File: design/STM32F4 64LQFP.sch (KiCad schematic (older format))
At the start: 15 parts, among them P2 SWD, U1 STM32F40X_LQFP64, X2 8MHz 10ppm

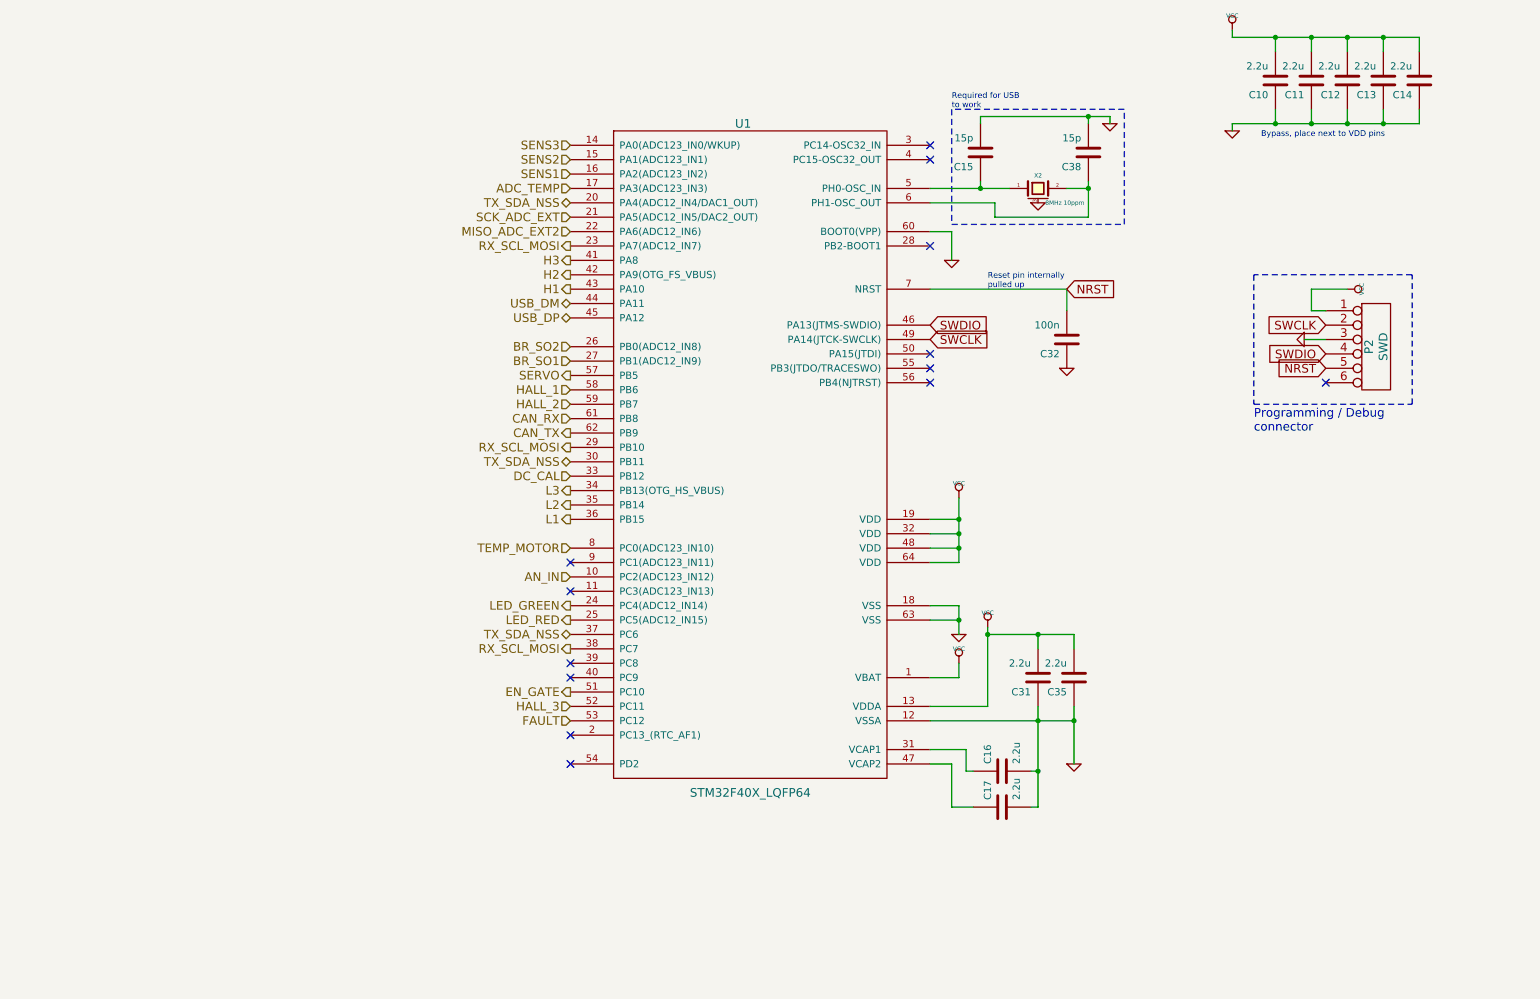
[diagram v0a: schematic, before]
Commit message: schema mods done
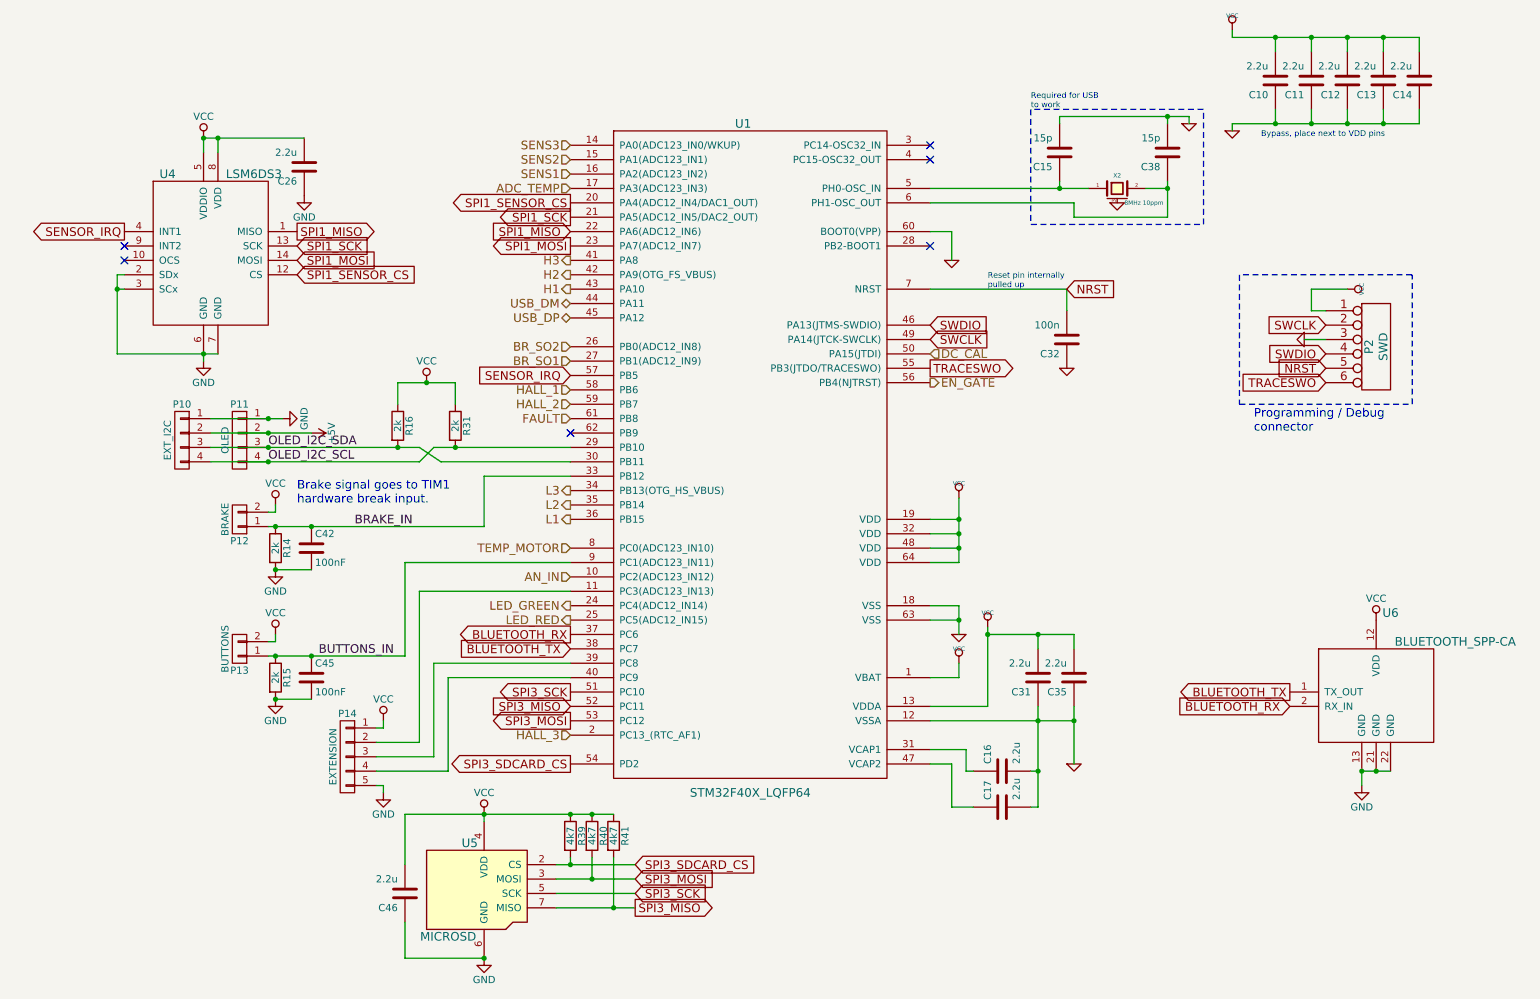
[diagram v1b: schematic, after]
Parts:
- added C26, C46: 2.2u, CRF1:SMD-0603_c, symbol C-RESCUE-BLDC_4
- added C42, C45: 100nF, symbol C
- added P10: EXT_I2C, symbol CONN_01X04
- added P11: OLED, symbol CONN_01X04
- added P12: BRAKE, symbol CONN_01X02
- added P13: BUTTONS, symbol CONN_01X02
- added P14: EXTENSION, symbol CONN_01X05
- added R14, R15, R16, R31: 2k, symbol R
- added R39, R40, R41: 4k7, symbol R
- added U4: LSM6DS3, symbol LSM6DS3
- added U5: MICROSD, symbol MICROSD
- added U6: BLUETOOTH_SPP-CA, symbol BLUETOOTH_SPP-CA
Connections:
- net CAN_RX is gone; now on net FAULT: U1.61 (PB8)
- net DC_CAL: now also U1.50 (PA15(JTDI)); no longer U1.33 (PB12)
- net EN_GATE: now also U1.56 (PB4(NJTRST)); no longer U1.51 (PC10)
- net FAULT: no longer U1.53 (PC12)
- net GND: now also C26.1, C42.2, C45.2, C46.1, P10.1 (P1), P11.1 (P1), P14.5 (P5), R14.2, R15.2, U4.2 (SDx), U4.3 (SCx), U4.6 (GND), U4.7 (GND), U5.6 (GND), U6.13 (GND), U6.21 (GND), U6.22 (GND)
- net HALL_3: now also U1.2 (PC13_(RTC_AF1)); no longer U1.52 (PC11)
- net VCC: now also C26.2, C46.2, P12.2 (P2), P13.2 (P2), P14.1 (P1), R16.1, R31.1, R39.1, R40.1, R41.1, U4.5 (VDDIO), U4.8 (VDD), U5.4 (VDD), U6.12 (VDD)
- net at U1.11 (PC3(ADC123_IN13)): now also P14.2 (P2)
- net at U1.39 (PC8): now also P14.3 (P3)
- net at U1.40 (PC9): now also P14.4 (P4)
- net SPI3_SDCARD_CS: now reaches U1.54 (PD2)
- net SPI3_SDCARD_CS: now also R39.2, U5.2 (CS)
- net TRACESWO: now reaches U1.55 (PB3(JTDO/TRACESWO))
- net TRACESWO: now also P2.6
- net BUTTONS_IN: now reaches U1.9 (PC1(ADC123_IN11))
- net BUTTONS_IN: now also C45.1, P13.1 (P1), R15.1
- net CAN_TX: no longer names the net of U1.62 (PB9)
- net MISO_ADC_EXT2 renamed SPI1_MISO
- net SPI1_MISO: now also U4.1 (MISO)
- removed net RX_SCL_MOSI: U1.23 (PA7(ADC12_IN7)), U1.29 (PB10), U1.38 (PC7)
- net SCK_ADC_EXT renamed SPI1_SCK
- net SPI1_SCK: now also U4.13 (SCK)
- net SERVO renamed SENSOR_IRQ
- net SENSOR_IRQ: now also U4.4 (INT1)
- removed net TX_SDA_NSS: U1.20 (PA4(ADC12_IN4/DAC1_OUT)), U1.30 (PB11), U1.37 (PC6)
- new net +5V: P10.2 (P2), P11.2 (P2)
- new net BLUETOOTH_RX: U1.37 (PC6), U6.2 (RX_IN)
- new net BLUETOOTH_TX: U1.38 (PC7), U6.1 (TX_OUT)
- new net BRAKE_IN: C42.1, P12.1 (P1), R14.1, U1.33 (PB12)
- new net OLED_I2C_SCL: P10.4 (P4), P11.4 (P4), R31.2, U1.29 (PB10)
- new net OLED_I2C_SDA: P10.3 (P3), P11.3 (P3), R16.2, U1.30 (PB11)
- new net SPI1_MOSI: U1.23 (PA7(ADC12_IN7)), U4.14 (MOSI)
- new net SPI1_SENSOR_CS: U1.20 (PA4(ADC12_IN4/DAC1_OUT)), U4.12 (CS)
- new net SPI3_MISO: R41.2, U1.52 (PC11), U5.7 (MISO)
- new net SPI3_MOSI: R40.2, U1.53 (PC12), U5.3 (MOSI)
- new net SPI3_SCK: U1.51 (PC10), U5.5 (SCK)
- no-connect marks 13 -> 6
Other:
- note added: "Brake signal goes to TIM1\nhardware break input."
- moved on the sheet: C15, C38, X2
